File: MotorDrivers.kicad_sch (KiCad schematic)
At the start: 0 parts

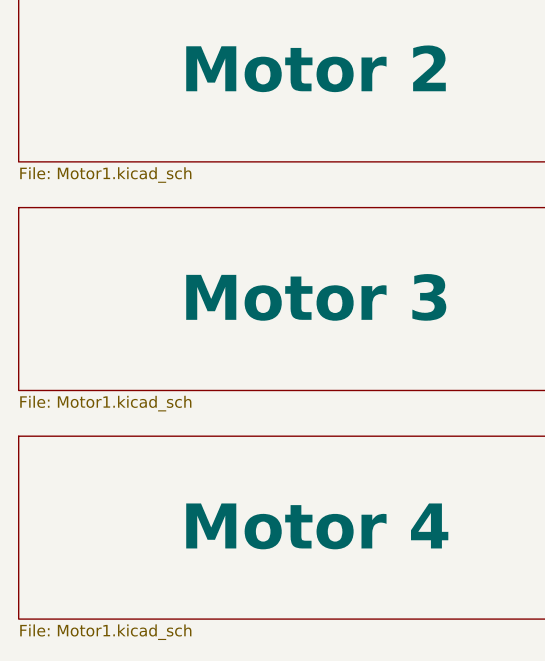
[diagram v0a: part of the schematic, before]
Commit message: Assigning a lot of values to components Change MOSFETS for different (correct) ones Copy Motor1 to Motor2-4 Guess max current per voltage on PowerSupply schema
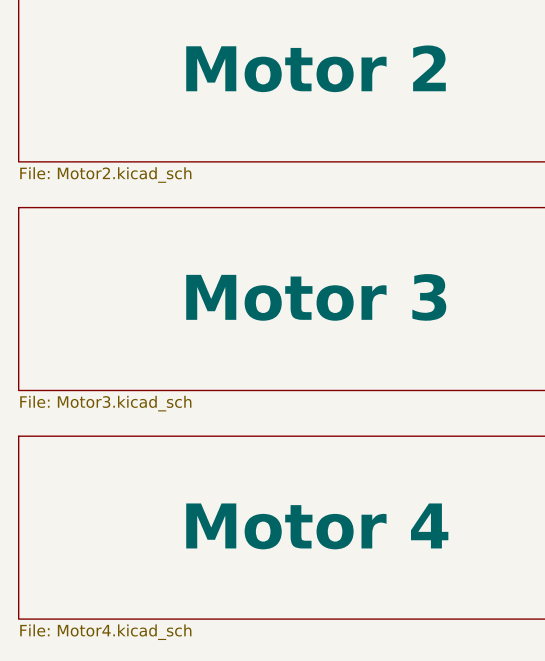
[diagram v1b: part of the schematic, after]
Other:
- sheet Motor 2: file Motor1.kicad_sch -> Motor2.kicad_sch
- sheet Motor 3: file Motor1.kicad_sch -> Motor3.kicad_sch
- sheet Motor 4: file Motor1.kicad_sch -> Motor4.kicad_sch
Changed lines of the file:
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@@
       (effects (font (size 5 5) bold))
     )
-    (property "Sheetfile" "Motor1.kicad_sch" (at 53.34 150.4446 0)
+    (property "Sheetfile" "Motor4.kicad_sch" (at 53.34 150.4446 0)
       (effects (font (size 1.27 1.27)) (justify left top))
     )
@@
       (effects (font (size 5 5) bold))
     )
-    (property "Sheetfile" "Motor1.kicad_sch" (at 53.34 125.0446 0)
+    (property "Sheetfile" "Motor3.kicad_sch" (at 53.34 125.0446 0)
       (effects (font (size 1.27 1.27)) (justify left top))
     )
@@
       (effects (font (size 5 5) bold))
     )
-    (property "Sheetfile" "Motor1.kicad_sch" (at 53.34 99.6446 0)
+    (property "Sheetfile" "Motor2.kicad_sch" (at 53.34 99.6446 0)
       (effects (font (size 1.27 1.27)) (justify left top))
     )

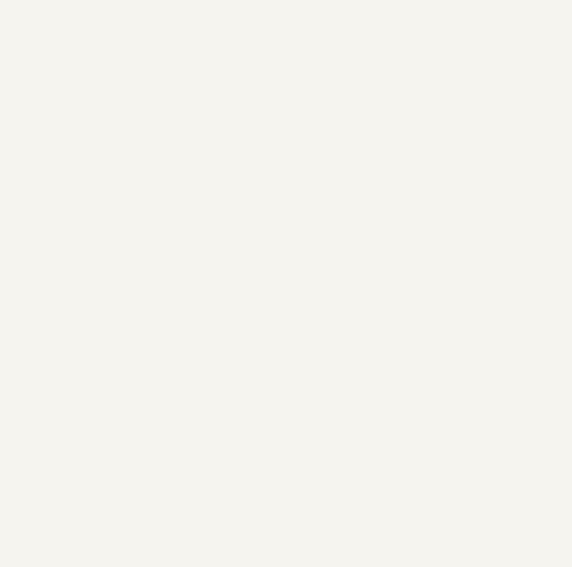
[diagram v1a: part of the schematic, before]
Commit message: Complete schematics Assign every value (very few exceptions) Change TCM5160 from on-board to separate module Add fuses Add power supplies (LDO + 2x buck converter)
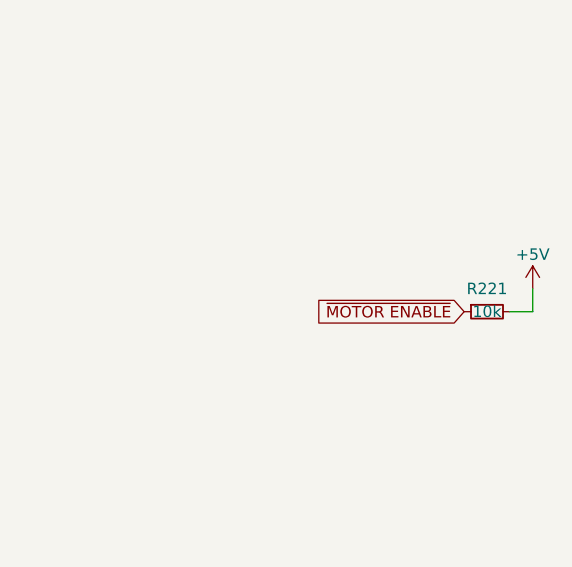
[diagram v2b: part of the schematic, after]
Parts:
- added R221: 10k, Resistor_SMD:R_0603_1608Metric, symbol Device:R_Small
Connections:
- new net +5V: R221.2
- new net ~{MOTOR ENABLE}: R221.1
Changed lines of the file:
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@@
     (company "Abit Gray")
+  )
+  (wire (pts (xy 195.58 95.25) (xy 195.58 97.79))
+    (stroke (width 0) (type default))
+  )
+  (wire (pts (xy 195.58 97.79) (xy 193.04 97.79))
+    (stroke (width 0) (type default))
+  )
+  (global_label "~{MOTOR ENABLE}" (shape input) (at 187.96 97.79 180) (fields_autoplaced)
+    (effects (font (size 1.27 1.27)) (justify right))
+    (property "Intersheetrefs" "${INTERSHEET_REFS}" (at 170.642 97.79 0)
+      (effects (font (size 1.27 1.27)) (justify right) hide)
+    )
+  )
+  (symbol (lib_id "Device:R_Small") (at 190.5 97.79 90) (mirror x) (unit 1)
+    (in_bom yes) (on_board yes) (dnp no)
+    (property "Reference" "R221" (at 190.5 95.25 90)
+      (effects (font (size 1.27 1.27)))
+    )
+    (property "Value" "10k" (at 190.5 97.79 90)
+      (effects (font (size 1.27 1.27)))
+    )
+    (property "Footprint" "Resistor_SMD:R_0603_1608Metric" (at 190.5 97.79 0)
+      (effects (font (size 1.27 1.27)) hide)
+    )
+    (property "Datasheet" "~" (at 190.5 97.79 0)
+      (effects (font (size 1.27 1.27)) hide)
+    )
+    (property "LCSC" "C25804" (at 190.5 97.79 0)
+      (effects (font (size 1.27 1.27)) hide)
+    )
+    (property "Mouser" "603-AC0603FR-1010KL" (at 190.5 97.79 0)
+      (effects (font (size 1.27 1.27)) hide)
+    )
+    (pin "1")
+    (pin "2")
+    (instances
+      (project "Can3DPrinter4Motor"
+        (path "/cb4e159a-5c17-494a-ba7f-10e700f814f1/e05e1111-b676-4692-8151-4de155805267"
+          (reference "R221") (unit 1)
+        )
+        (path "/cb4e159a-5c17-494a-ba7f-10e700f814f1/03ab3e80-f454-40c8-8f97-43a0b791de0b"
+          (reference "R501") (unit 1)
+        )
+      )
+    )
+  )
+  (symbol (lib_id "power:+5V") (at 195.58 95.25 0) (unit 1)
+    (in_bom yes) (on_board yes) (dnp no)
+    (property "Reference" "#PWR0517" (at 195.58 99.06 0)
+      (effects (font (size 1.27 1.27)) hide)
+    )
+    (property "Value" "+5V" (at 195.58 91.44 0)
+      (effects (font (size 1.27 1.27)))
+    )
+    (property "Footprint" "" (at 195.58 95.25 0)
+      (effects (font (size 1.27 1.27)) hide)
+    )
+    (property "Datasheet" "" (at 195.58 95.25 0)
+      (effects (font (size 1.27 1.27)) hide)
+    )
+    (pin "1")
+    (instances
+      (project "Can3DPrinter4Motor"
+        (path "/cb4e159a-5c17-494a-ba7f-10e700f814f1/03ab3e80-f454-40c8-8f97-43a0b791de0b"
+          (reference "#PWR0517") (unit 1)
+        )
+      )
+    )
   )
   (sheet (at 53.34 129.54) (size 66.04 20.32)

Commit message: Finish PCB, documentation
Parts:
- added R221: 10k, Resistor_SMD:R_0603_1608Metric, symbol Device:R_Small
- R221: now not fitted; now left out of the parts list
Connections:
- net ~{MOTOR ENABLE}: now also R221.1
- new net GND: R221.2
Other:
- note added: "Disable"
- note added: "Enable"
- note added: "by default"
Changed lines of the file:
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@@
     (company "Abit Gray")
   )
+  (junction (at 186.69 99.06) (diameter 0) (color 0 0 0 0)
+  )
+  (wire (pts (xy 186.69 99.06) (xy 186.69 100.33))
+    (stroke (width 0) (type default))
+  )
   (wire (pts (xy 195.58 95.25) (xy 195.58 97.79))
+    (stroke (width 0) (type default))
+  )
+  (wire (pts (xy 186.69 97.79) (xy 187.96 97.79))
+    (stroke (width 0) (type default))
+  )
+  (wire (pts (xy 186.69 97.79) (xy 186.69 99.06))
+    (stroke (width 0) (type default))
+  )
+  (wire (pts (xy 195.58 100.33) (xy 195.58 102.87))
+    (stroke (width 0) (type default))
+  )
+  (wire (pts (xy 185.42 99.06) (xy 186.69 99.06))
+    (stroke (width 0) (type default))
+  )
+  (wire (pts (xy 193.04 100.33) (xy 195.58 100.33))
+    (stroke (width 0) (type default))
+  )
+  (wire (pts (xy 187.96 100.33) (xy 186.69 100.33))
     (stroke (width 0) (type default))
   )
@@
     (stroke (width 0) (type default))
   )
-  (global_label "~{MOTOR ENABLE}" (shape input) (at 187.96 97.79 180) (fields_autoplaced)
+  (text "Disable" (at 195.58 97.79 0)
+    (effects (font (size 1.27 1.27)) (justify left bottom))
+  )
+  (text "by default" (at 203.2 100.33 0)
+    (effects (font (size 1.27 1.27)) (justify left bottom))
+  )
+  (text "Enable" (at 195.58 101.6 0)
+    (effects (font (size 1.27 1.27)) (justify left bottom))
+  )
+  (global_label "~{MOTOR ENABLE}" (shape input) (at 185.42 99.06 180) (fields_autoplaced)
     (effects (font (size 1.27 1.27)) (justify right))
-    (property "Intersheetrefs" "${INTERSHEET_REFS}" (at 170.642 97.79 0)
+    (property "Intersheetrefs" "${INTERSHEET_REFS}" (at 168.102 99.06 0)
       (effects (font (size 1.27 1.27)) (justify right) hide)
     )
   )
   (symbol (lib_id "Device:R_Small") (at 190.5 97.79 90) (mirror x) (unit 1)
-    (in_bom yes) (on_board yes) (dnp no)
+    (in_bom no) (on_board yes) (dnp yes)
     (property "Reference" "R221" (at 190.5 95.25 90)
       (effects (font (size 1.27 1.27)))
@@
         )
       )
+    )
+  )
+  (symbol (lib_id "Device:R_Small") (at 190.5 100.33 90) (unit 1)
+    (in_bom yes) (on_board yes) (dnp no)
+    (property "Reference" "R221" (at 190.5 102.87 90)
+      (effects (font (size 1.27 1.27)))
+    )
+    (property "Value" "10k" (at 190.5 100.33 90)
+      (effects (font (size 1.27 1.27)))
+    )
+    (property "Footprint" "Resistor_SMD:R_0603_1608Metric" (at 190.5 100.33 0)
+      (effects (font (size 1.27 1.27)) hide)
+    )
+    (property "Datasheet" "~" (at 190.5 100.33 0)
+      (effects (font (size 1.27 1.27)) hide)
+    )
+    (property "LCSC" "C25804" (at 190.5 100.33 0)
+      (effects (font (size 1.27 1.27)) hide)
+    )
+    (property "Mouser" "603-AC0603FR-1010KL" (at 190.5 100.33 0)
+      (effects (font (size 1.27 1.27)) hide)
+    )
+    (pin "1")
+    (pin "2")
+    (instances
+      (project "4MotorCAN"
+        (path "/cb4e159a-5c17-494a-ba7f-10e700f814f1/e05e1111-b676-4692-8151-4de155805267"
+          (reference "R221") (unit 1)
+        )
+        (path "/cb4e159a-5c17-494a-ba7f-10e700f814f1/03ab3e80-f454-40c8-8f97-43a0b791de0b"
+          (reference "R502") (unit 1)
+        )
+      )
+    )
+  )
+  (symbol (lib_id "power:GND") (at 195.58 102.87 0) (unit 1)
+    (in_bom yes) (on_board yes) (dnp no)
+    (property "Reference" "#PWR0505" (at 195.58 109.22 0)
+      (effects (font (size 1.27 1.27)) hide)
+    )
+    (property "Value" "GND" (at 195.58 106.68 0)
+      (effects (font (size 1.27 1.27)))
+    )
+    (property "Footprint" "" (at 195.58 102.87 0)
+      (effects (font (size 1.27 1.27)) hide)
+    )
+    (property "Datasheet" "" (at 195.58 102.87 0)
+      (effects (font (size 1.27 1.27)) hide)
+    )
+    (pin "1")
+    (instances
+      (project "4MotorCAN"
+        (path "/cb4e159a-5c17-494a-ba7f-10e700f814f1/03ab3e80-f454-40c8-8f97-43a0b791de0b"
+          (reference "#PWR0505") (unit 1)
+        )
+      )
